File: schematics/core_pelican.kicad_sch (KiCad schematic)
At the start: 20 parts, among them J5 61300411121, SW2 PTS526SK15SMTR2LFS, SW3 PTS526SK15SMTR2LFS, U0 Core1106

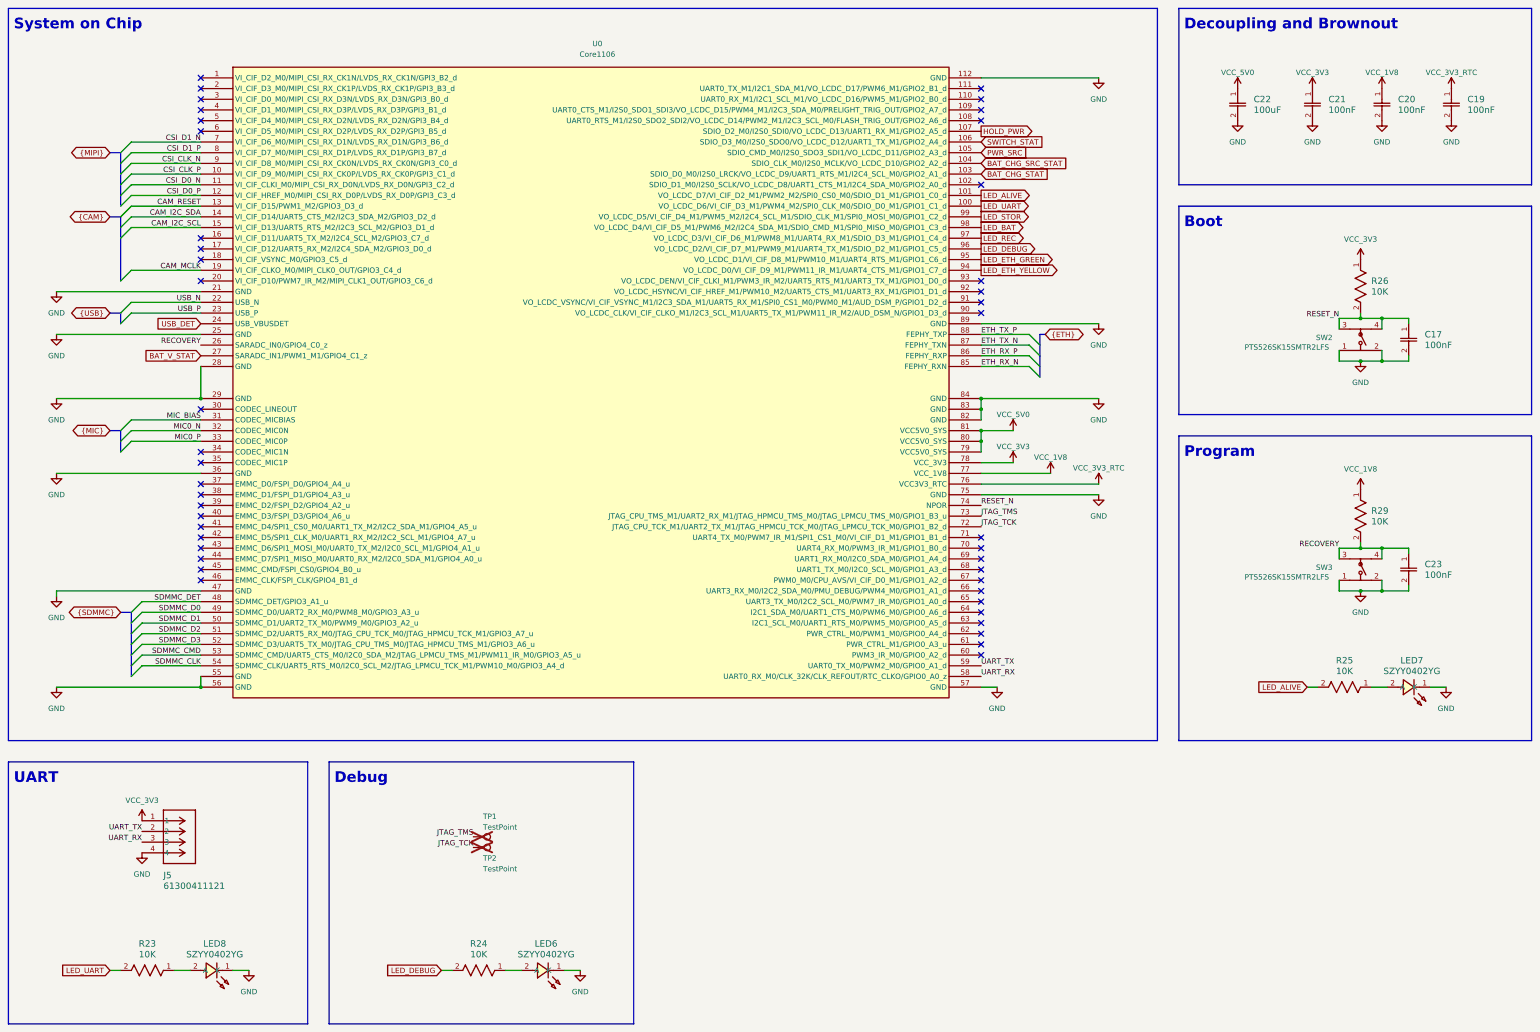
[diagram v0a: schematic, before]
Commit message: updated schematic based on review
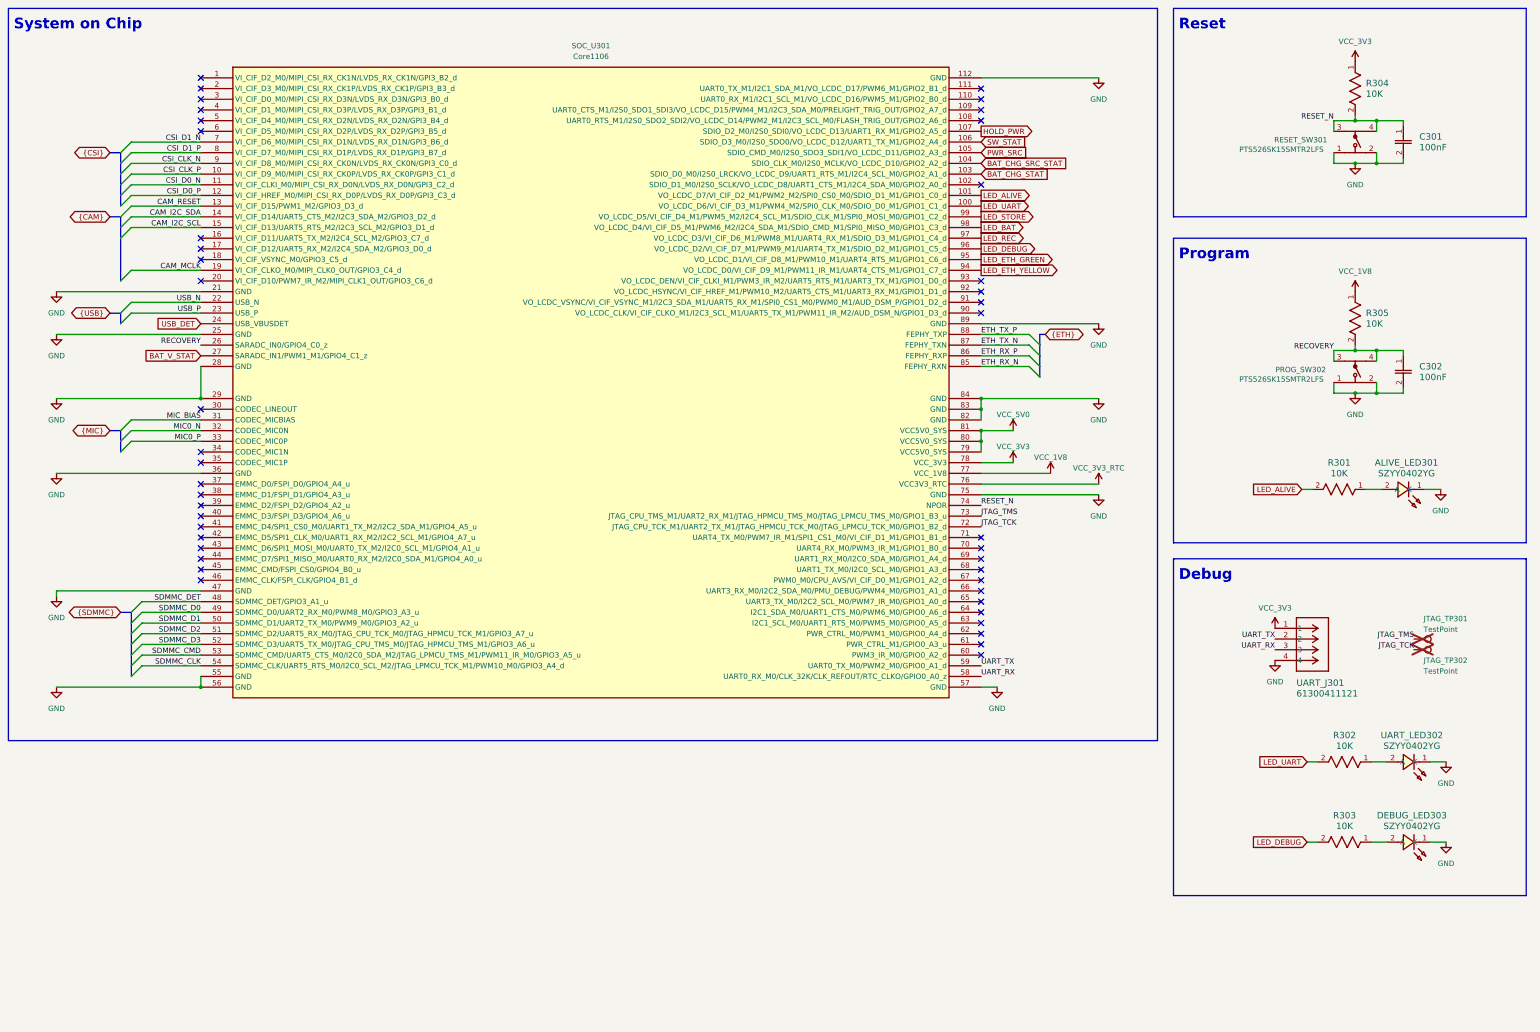
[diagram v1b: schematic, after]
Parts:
- removed C19, C20, C21: 100nF, C_GRM155R71C104KA88D:C_GRM155R71C104KA88D, symbol C_GRM155R71C104KA88D:GRM155R71C104KA88D
- removed C22: 100uF, C_EMK325ABJ107MM-T:C_EMK325ABJ107MM-T, symbol C_EMK325ABJ107MM-T:EMK325ABJ107MM-T
- renumbered LED7 to ALIVE_LED301, C17 to C301, C23 to C302, LED6 to DEBUG_LED303, TP1 to JTAG_TP301, TP2 to JTAG_TP302, SW3 to PROG_SW302, R25 to R301, R23 to R302, R24 to R303, R26 to R304, R29 to R305, SW2 to RESET_SW301, U0 to SOC_U301, J5 to UART_J301, LED8 to UART_LED302
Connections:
- net LED_STOR renamed LED_STORE
- net SWITCH_STAT renamed SW_STAT
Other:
- note added: "Reset"
- note removed: "Boot"
- note removed: "Decoupling and Brownout"
- note removed: "UART"
- moved on the sheet: ALIVE_LED301, C301, C302, DEBUG_LED303, JTAG_TP301, JTAG_TP302, PROG_SW302, R301, R302, R303, R304, R305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
